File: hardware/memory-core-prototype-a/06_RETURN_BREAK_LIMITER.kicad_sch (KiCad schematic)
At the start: 1 part, among them J906 SHEET_INTERFACE_NOT_FITTED

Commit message: Capture ERC-validated Return Break limiter sheet
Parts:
- removed J906: SHEET_INTERFACE_NOT_FITTED, symbol Connector_Generic:Conn_01x07
- added C600: 1.2nF stability, Capacitor_SMD:C_0805_2012Metric, symbol Device:C
- added C601: 100nF V+, Capacitor_SMD:C_0805_2012Metric, symbol Device:C
- added C6010, C606: 4.7uF - rail, Capacitor_SMD:C_0805_2012Metric, symbol Device:C
- added C602: 100nF V-, Capacitor_SMD:C_0805_2012Metric, symbol Device:C
- added C603, C607: 100nF + rail, Capacitor_SMD:C_0805_2012Metric, symbol Device:C
- added C604, C608: 100nF - rail, Capacitor_SMD:C_0805_2012Metric, symbol Device:C
- added C605, C609: 4.7uF + rail, Capacitor_SMD:C_0805_2012Metric, symbol Device:C
- added C611: 100pF I/V, Capacitor_SMD:C_0805_2012Metric, symbol Device:C
- added C612: 1nF Break blur, Capacitor_SMD:C_0805_2012Metric, symbol Device:C
- added C613: 1uF +ref, Capacitor_SMD:C_0805_2012Metric, symbol Device:C
- added C614: 1uF -ref, Capacitor_SMD:C_0805_2012Metric, symbol Device:C
- added C615: 4.7uF release, Capacitor_SMD:C_0805_2012Metric, symbol Device:C
- added D600, D601: BAV199-class soft clip, symbol Device:D
- added D602: BAT54-class high clamp, symbol Device:D_Schottky
- added D603: BAT54-class low clamp, symbol Device:D_Schottky
- added D604: BAT54-class precision rectifier, symbol Device:D_Schottky
- added D605: 3.0V control clamp provisional, symbol Device:D_Zener
- added R600: 20k input, Resistor_SMD:R_0805_2012Metric, symbol Device:R
- added R601: 220R stability, Resistor_SMD:R_0805_2012Metric, symbol Device:R
- added R602: 20k I/V, Resistor_SMD:R_0805_2012Metric, symbol Device:R
- added R603: 22k Break input, Resistor_SMD:R_0805_2012Metric, symbol Device:R
- added R604: 22k Break feedback, Resistor_SMD:R_0805_2012Metric, symbol Device:R
- added R605: 22k normalise input, Resistor_SMD:R_0805_2012Metric, symbol Device:R
- added R606: 22k normalise feedback, Resistor_SMD:R_0805_2012Metric, symbol Device:R
- added R607: 38k +ref top, Resistor_SMD:R_0805_2012Metric, symbol Device:R
- added R608: 10k +ref bottom, Resistor_SMD:R_0805_2012Metric, symbol Device:R
- added R609: 38k -ref top, Resistor_SMD:R_0805_2012Metric, symbol Device:R
- added R610: 10k -ref bottom, Resistor_SMD:R_0805_2012Metric, symbol Device:R
- added R611: 2.2k, Resistor_SMD:R_0805_2012Metric, symbol Device:R
- added R612: 40.2k, Resistor_SMD:R_0805_2012Metric, symbol Device:R
- added R613: 27.4k, Resistor_SMD:R_0805_2012Metric, symbol Device:R
- added R614: 10k attack, Resistor_SMD:R_0805_2012Metric, symbol Device:R
- added R615: 220k release, Resistor_SMD:R_0805_2012Metric, symbol Device:R
- added TP600: RETURN_DAC, symbol Connector:TestPoint
- added TP601: RETURN_VCA, symbol Connector:TestPoint
- added TP602: BREAK_OUT, symbol Connector:TestPoint
- added TP603: RETURN_NORM, symbol Connector:TestPoint
- added TP604: +2V5_REF, symbol Connector:TestPoint
- added TP605: -2V5_REF, symbol Connector:TestPoint
- added TP606: RETURN_LIMITED, symbol Connector:TestPoint
- added TP607: RETURN_FEED, symbol Connector:TestPoint
- added TP608: ABSENCE_INFLUENCE, symbol Connector:TestPoint
- added TP609: VCA_RETURN_CTRL, symbol Connector:TestPoint
- added U50: SSI2164, symbol MerrinLab_PrototypeA:SSI2164S_APPLICATION
- added U60: OPA1679 RETURN A, symbol MerrinLab_PrototypeA:OPA1679_PW_APPLICATION
- added U61: OPA1679 RETURN B, symbol MerrinLab_PrototypeA:OPA1679_PW_APPLICATION
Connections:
- net ABSENCE_INFLUENCE: now also C615.1, D605.1 (K), R614.2, R615.1, TP608.1
- net RAIL_N12: now also C6010.1, C602.1, C604.1, C606.1, C608.1, R609.1, U50.9 (V-), U60.11 (V-), U61.11 (V-)
- net RAIL_P12: now also C601.1, C603.1, C605.1, C607.1, C609.1, R607.1, U50.16 (V+), U60.4 (V+), U61.4 (V+)
- net RETURN_DAC: now also R600.1, TP600.1
- net RETURN_FEED: now also R613.1, TP607.1, U61.8 (OUT_C)
- net RETURN_LIMITED: now also R612.1, TP606.1, U61.12 (IN_D+), U61.6 (IN_B-), U61.7 (OUT_B)
- net VCA_RETURN_CTRL: now also TP609.1, U50.11 (VC3)
- new net ABS_RECT: D604.1 (K), R614.1, U61.13 (IN_D-)
- new net ABS_RECT_DRIVE: D604.2 (A), U61.14 (OUT_D)
- new net BREAK_OUT: C612.1, D600.1 (K), D601.2 (A), R604.1, R605.1, TP602.1, U60.7 (OUT_B)
- new net BREAK_SUM: C612.2, D600.2 (A), D601.1 (K), R603.2, R604.2, U60.6 (IN_B-)
- new net GND: C600.2, C601.2, C6010.2, C602.2, C603.2, C604.2, C605.2, C606.2, C607.2, C608.2, C609.2, C613.2, C614.2, C615.2, D605.2 (A), R608.2, R610.2, R615.2, U50.8 (GND), U60.10 (IN_C+), U60.3 (IN_A+), U60.5 (IN_B+), U61.10 (IN_C+)
- new net REF_N2V5: D603.2 (A), TP605.1, U61.1 (OUT_A), U61.2 (IN_A-)
- new net REF_N_DIV: C614.1, R609.2, R610.1, U61.3 (IN_A+)
- new net REF_P2V5: D602.1 (K), TP604.1, U60.13 (IN_D-), U60.14 (OUT_D)
- new net REF_P_DIV: C613.1, R607.2, R608.1, U60.12 (IN_D+)
- new net RETFEED_SUM: R612.2, R613.2, U61.9 (IN_C-)
- new net RETURN_CLAMP: D602.2 (A), D603.1 (K), R611.2, U61.5 (IN_B+)
- new net RETURN_NORM: R606.1, R611.1, TP603.1, U60.8 (OUT_C)
- new net RETURN_VCA: C611.1, R602.1, R603.1, TP601.1, U60.1 (OUT_A)
- new net RET_NORM_SUM: R605.2, R606.2, U60.9 (IN_C-)
- new net SSI_IIN3: R600.2, R601.1, U50.10 (IIN3)
- new net SSI_IOUT3: C611.2, R602.2, U50.12 (IOUT3), U60.2 (IN_A-)
- new net SSI_RC3: C600.1, R601.2
- no-connect marks 0 -> 10
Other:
- note added: "Clamp references +/-2.5 V plus Schottky Vf give approximately 5.4-5.6 Vpp RETURN_LIMITED. Fixed feed magnitude = 27.4k / 40.2k = 0.6816; 1% worst case < 0.696."
- note added: "SSI2164 CH3: pins 10 IIN3, 11 VC3, 12 IOUT3. MODE pin 1 open = Class AB. Current output is converted by U60A; it is not treated as a voltage output."
- note added: "SSI2164 RETURN VCA • BOUNDED BREAK • INDEPENDENT HARD CLAMP • FIXED FEED"
- note added: "Small-signal path: SSI VCA <= unity; Break = -1; normaliser = -1. Only RETURN_LIMITED, RETURN_FEED and bounded ABSENCE_INFLUENCE cross this sheet."
- note added: "U50 units A/B/D are reserved no-connect placeholders on sheet 06. Sheet 05 must remove these placeholders and place the real Memory/Ghost/Wet channels."
- note added: "U50/U60/U61 and clamp-diode footprints intentionally blank. Exact diode leakage/Vf, reference source/sink current, measured loop gain and 30-minute endurance remain gates."
- note removed: "HIERARCHY / INTERFACE CAPTURE ONLY — CIRCUIT CONTENT NOT YET ACCEPTED"
- title: Memory Core Prototype A — RETURN / BREAK / LIMITER -> Memory Core Prototype A — Return / Break / Limiter

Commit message: Capture ERC-validated Return Break limiter sheet
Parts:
- removed C6010, C606: 4.7uF - rail, Capacitor_SMD:C_0805_2012Metric, symbol Device:C
- removed C602: 100nF V-, Capacitor_SMD:C_0805_2012Metric, symbol Device:C
- removed C604, C608: 100nF - rail, Capacitor_SMD:C_0805_2012Metric, symbol Device:C
- removed C605, C609: 4.7uF + rail, Capacitor_SMD:C_0805_2012Metric, symbol Device:C
- removed C607: 100nF + rail, Capacitor_SMD:C_0805_2012Metric, symbol Device:C
- removed D600, D601: BAV199-class soft clip, symbol Device:D
- removed D602: BAT54-class high clamp, symbol Device:D_Schottky
- removed D603: BAT54-class low clamp, symbol Device:D_Schottky
- removed D604: BAT54-class precision rectifier, symbol Device:D_Schottky
- removed D605: 3.0V control clamp provisional, symbol Device:D_Zener
- removed R606: 22k normalise feedback, Resistor_SMD:R_0805_2012Metric, symbol Device:R
- removed R607: 38k +ref top, Resistor_SMD:R_0805_2012Metric, symbol Device:R
- removed R608: 10k +ref bottom, Resistor_SMD:R_0805_2012Metric, symbol Device:R
- removed R609: 38k -ref top, Resistor_SMD:R_0805_2012Metric, symbol Device:R
- removed R615: 220k release, Resistor_SMD:R_0805_2012Metric, symbol Device:R
- removed U50: SSI2164, symbol MerrinLab_PrototypeA:SSI2164S_APPLICATION
- removed U60: OPA1679 RETURN A, symbol MerrinLab_PrototypeA:OPA1679_PW_APPLICATION
- added C610: 100nF + rail, Capacitor_SMD:C_0805_2012Metric, symbol Device:C
- added C616: 4.7uF + rail, Capacitor_SMD:C_0805_2012Metric, symbol Device:C
- added C617: 4.7uF - rail, Capacitor_SMD:C_0805_2012Metric, symbol Device:C
- added C618: 100nF SSI + rail, Capacitor_SMD:C_0805_2012Metric, symbol Device:C
- added C619: 100nF SSI - rail, Capacitor_SMD:C_0805_2012Metric, symbol Device:C
- added C620, C621: 1uF, Capacitor_SMD:C_0805_2012Metric, symbol Device:C
- added C630: 1uF attack/release, Capacitor_SMD:C_0805_2012Metric, symbol Device:C
- added C640: 330pF bandwidth, Capacitor_SMD:C_0805_2012Metric, symbol Device:C
- added C641: 390pF bandwidth loss, Capacitor_SMD:C_0805_2012Metric, symbol Device:C
- added D600, D610: BAT54-class upper clamp, symbol Device:D_Schottky
- added D601, D611: BAT54-class lower clamp, symbol Device:D_Schottky
- added D602: Break diode A, symbol Device:D
- added D603: Break diode B, symbol Device:D
- added D604: Asym single, symbol Device:D
- added D605: Asym pair 1, symbol Device:D
- added D606: Asym pair 2, symbol Device:D
- added D607: Upper hard clamp, symbol Device:D_Schottky
- added D608: Lower hard clamp, symbol Device:D_Schottky
- added D609: Envelope rectifier, symbol Device:D_Schottky
- added D612: Fault-neutral clamp, symbol Device:D_Schottky
- added R620, R622: 38.3k 1%, Resistor_SMD:R_0805_2012Metric, symbol Device:R
- added R621, R623: 10k 1%, Resistor_SMD:R_0805_2012Metric, symbol Device:R
- added R624: 2.2k clamp current, Resistor_SMD:R_0805_2012Metric, symbol Device:R
- added R625: 47R output isolate, Resistor_SMD:R_0805_2012Metric, symbol Device:R
- added R626: 40.2k 1%, Resistor_SMD:R_0805_2012Metric, symbol Device:R
- added R627: 27.4k 1%, Resistor_SMD:R_0805_2012Metric, symbol Device:R
- added R630: 10k rectifier feed, Resistor_SMD:R_0805_2012Metric, symbol Device:R
- added R631: 100k release, Resistor_SMD:R_0805_2012Metric, symbol Device:R
- added R632: 1k output isolate, Resistor_SMD:R_0805_2012Metric, symbol Device:R
- added R633: 100k neutral pull-down, Resistor_SMD:R_0805_2012Metric, symbol Device:R
- added RV60: 100k BREAK AMOUNT, symbol MerrinLab_PrototypeA:R_POT_123
- added TP610: SSI_VC3, symbol Connector:TestPoint
- added U60: SSI2164, symbol MerrinLab_PrototypeA:SSI2164S_MULTI
- added U62: OPA1679 REFERENCES / ABSENCE, symbol MerrinLab_PrototypeA:OPA1679_PW_APPLICATION
- C600: value 1.2nF stability -> 10uF AC; footprint Capacitor_SMD:C_0805_2012Metric -> (none)
- C601: value 100nF V+ -> 1.2nF stability
- C603: value 100nF + rail -> 100pF I/V
- C611: value 100pF I/V -> 100nF - rail
- C612: value 1nF Break blur -> 4.7uF + rail
- C613: value 1uF +ref -> 4.7uF - rail
- C614: value 1uF -ref -> 100nF + rail
- C615: value 4.7uF release -> 100nF - rail
- R600: value 20k input -> 20k
- R601: value 220R stability -> 10k
- R602: value 20k I/V -> 20k SSI input
- R603: value 22k Break input -> 220R stability
- R604: value 22k Break feedback -> 1k control isolate
- R605: value 22k normalise input -> 20k I/V
- R610: value 10k -ref bottom -> 20k
- R611: value 2.2k -> 20k unity feedback
- R612: value 40.2k -> 20k
- R613: value 27.4k -> 20k unity feedback
- R614: value 10k attack -> 6.8k nonlinear feed
- TP601: value RETURN_VCA -> RETURN_NORM
- TP602: value BREAK_OUT -> RETURN_VCA
- TP603: value RETURN_NORM -> BREAK
- TP604: value +2V5_REF -> RETURN_NONLINEAR
- TP605: value -2V5_REF -> +2V5_REF
- TP606: value RETURN_LIMITED -> -2V5_REF
- TP607: value RETURN_FEED -> RETURN_LIMITED
- TP608: value ABSENCE_INFLUENCE -> RETURN_FEED
- TP609: value VCA_RETURN_CTRL -> ABSENCE_INFLUENCE
- U61: value OPA1679 RETURN B -> OPA1679 RETURN AUDIO
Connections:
- net ABS_RECT_DRIVE is gone; now on net RET_LIM_BUF: U61.14 (OUT_D)
- net REF_P_DIV is gone; now on net RAIL_N12: C613.1
- net RET_NORM_SUM is gone; now on net SSI_IOUT3: R605.2
- net ABSENCE_INFLUENCE: now also TP609.1, D610.2 (A), D611.1 (K), D612.2 (A), R632.2, R633.1; no longer C615.1, R614.2, TP608.1
- net GND: now also C611.2, C612.2, R601.2, U61.3 (IN_A+), U61.5 (IN_B+), C610.2, C616.2, C617.2, C618.2, C619.2, C620.2, C621.2, C630.2, D601.2 (A), D611.2 (A), R621.2, R623.2, R631.2, R633.2, U60.8 (GND), U62.10 (IN_C+); no longer C600.2, C603.2, R610.2
- net RAIL_N12: now also C611.1, C615.1, C617.1, C619.1, R622.1, U60.9 (V-), U62.11 (V-)
- net RAIL_P12: now also C612.1, C614.1, C610.1, C616.1, C618.1, R620.1, U60.16 (V+), U62.4 (V+); no longer C601.1, C603.1
- net REF_N2V5: now also TP606.1, D608.2 (A), U62.6 (IN_B-), U62.7 (OUT_B); no longer TP605.1, U61.1 (OUT_A), U61.2 (IN_A-)
- net REF_P2V5: now also TP605.1, D607.1 (K), U62.1 (OUT_A), U62.2 (IN_A-); no longer TP604.1
- net RETFEED_SUM: now also R626.2, R627.2, U62.9 (IN_C-); no longer R612.2, R613.2, U61.9 (IN_C-)
- net RETURN_FEED: now also TP608.1, R627.1, U62.8 (OUT_C); no longer R613.1, TP607.1, U61.8 (OUT_C)
- net RETURN_LIMITED: now also TP607.1, R625.2, R626.1, R630.1; no longer R612.1, TP606.1, U61.12 (IN_D+), U61.6 (IN_B-), U61.7 (OUT_B)
- net RETURN_VCA: now also C603.1, R605.1, R610.1, TP602.1, U61.1 (OUT_A); no longer C611.1, R602.1, R603.1, TP601.1
- net SSI_IIN3: now also R602.2, R603.1, U60.15 (IIN3); no longer R600.2, R601.1
- net SSI_IOUT3: now also C603.2, U61.2 (IN_A-), U60.13 (IOUT3); no longer C611.2, R602.2
- net VCA_RETURN_CTRL: now also R604.1; no longer TP609.1
- net ABS_RECT renamed RET_LIM_BUF
- net RET_LIM_BUF: now also R625.1; no longer R614.1
- removed net BREAK_OUT: C612.1, R604.1, R605.1, TP602.1
- removed net BREAK_SUM: C612.2, R603.2, R604.2
- removed net REF_N_DIV: C614.1, R610.1, U61.3 (IN_A+)
- net RETURN_CLAMP renamed BRK_SUM
- net BRK_SUM: now also R610.2, U61.6 (IN_B-), C640.2, RV60.3 (END_B); no longer U61.5 (IN_B+)
- net RETURN_NORM renamed BRK_OUT
- net BRK_OUT: now also R612.1, U61.7 (OUT_B), C640.1, D602.1 (K), D603.2 (A)
- net SSI_RC3 renamed RETURN_DIV
- net RETURN_DIV: now also R600.2, R601.1, TP601.1; no longer R601.2
- new net ABS_CTRL_DRV: R632.1, U62.13 (IN_D-), U62.14 (OUT_D)
- new net ABS_ENV_RAW: C630.1, D609.1 (K), R631.1, U62.12 (IN_D+)
- new net ABS_RECT_IN: D609.2 (A), R630.2
- new net BRK_DIODE: D602.2 (A), D603.1 (K), RV60.1 (END_A), RV60.2 (WIPER)
- new net HARDWARE_FAULT_N: D612.1 (K)
- new net RAIL_3V3: D600.1 (K), D610.1 (K)
- new net REFN_DIV: C621.1, R622.2, R623.1, U62.5 (IN_B+)
- new net REFP_DIV: C620.1, R620.2, R621.1, U62.3 (IN_A+)
- new net RETURN_VCA_AC: C600.2, R602.1
- new net RET_ASYM_A: D604.2 (A), D605.1 (K), R614.2
- new net RET_ASYM_B: D605.2 (A), D606.1 (K)
- new net RET_CLAMP_NODE: D607.2 (A), D608.1 (K), R624.2, U61.12 (IN_D+)
- new net RET_NL_OUT: C641.1, R613.1, R614.1, R624.1, TP604.1, U61.8 (OUT_C)
- new net RET_SUM: C641.2, D604.1 (K), D606.2 (A), R612.2, R613.2, U61.9 (IN_C-)
- new net SSI_STAB3: C601.1, R603.2
- new net SSI_VC3: D600.2 (A), D601.1 (K), R604.2, TP610.1, U60.14 (VC3)
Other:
- note added: "FIXED FEED: 27.4k / 40.2k = 0.6816 nominal; 1% worst case <0.696. Only RETURN_LIMITED, RETURN_FEED and ABSENCE_INFLUENCE cross this boundary."
- note added: "GAIN CONTRACT sheet-03 Return receiver ~0.747; R600/R601 = 1/3; combined ~0.249. SSI2164 VC3 is restricted to 0…3.3 V, so VCA gain cannot exceed unity. Break and RET-01 are unity at small signal; nonlinear branches alter shape, not linear gain."
- note added: "HARD LIMITER R624 limits clamp current. D607/D608 clamp to buffered +/-2.5 V references. Expected first-pass limit ~+/-2.7…2.8 V. Limiter remains analogue and MCU-independent."
- note added: "Official SSI2164 channel 3 pins: 15 IIN3, 14 VC3, 13 IOUT3. Pins 10/11/12 are channel 4 and are reserved for the wet-master unit on sheet 05."
- note added: "SSI2164 CH3 • VARIABLE BREAK • UNITY-NORMALISED RETURN • INDEPENDENT ANALOGUE CLAMP"
- note added: "U60 units 1, 2 and 4 are visible staged reservations for sheet 05. They are the same physical SSI2164 as units 3 and 5, not duplicate chips. Sheet 05 must remove these reservations and place the real Memory/Ghost/Wet circuits."
- note removed: "Clamp references +/-2.5 V plus Schottky Vf give approximately 5.4-5.6 Vpp RETURN_LIMITED. Fixed feed magnitude = 27.4k / 40.2k = 0.6816; 1% worst case < 0.696."
- note removed: "SSI2164 CH3: pins 10 IIN3, 11 VC3, 12 IOUT3. MODE pin 1 open = Class AB. Current output is converted by U60A; it is not treated as a voltage output."
- note removed: "SSI2164 RETURN VCA • BOUNDED BREAK • INDEPENDENT HARD CLAMP • FIXED FEED"
- note removed: "Small-signal path: SSI VCA <= unity; Break = -1; normaliser = -1. Only RETURN_LIMITED, RETURN_FEED and bounded ABSENCE_INFLUENCE cross this sheet."
- note removed: "U50 units A/B/D are reserved no-connect placeholders on sheet 06. Sheet 05 must remove these placeholders and place the real Memory/Ghost/Wet channels."
- note removed: "U50/U60/U61 and clamp-diode footprints intentionally blank. Exact diode leakage/Vf, reference source/sink current, measured loop gain and 30-minute endurance remain gates."

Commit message: Capture ERC-validated Memory Ghost wet sheet
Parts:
- removed unit 1 of U60
- removed unit 2 of U60
- removed unit 4 of U60
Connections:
- no-connect marks 10 -> 1
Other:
- note removed: "U60 units 1, 2 and 4 are visible staged reservations for sheet 05. They are the same physical SSI2164 as units 3 and 5, not duplicate chips. Sheet 05 must remove these reservations and place the real Memory/Ghost/Wet circuits."

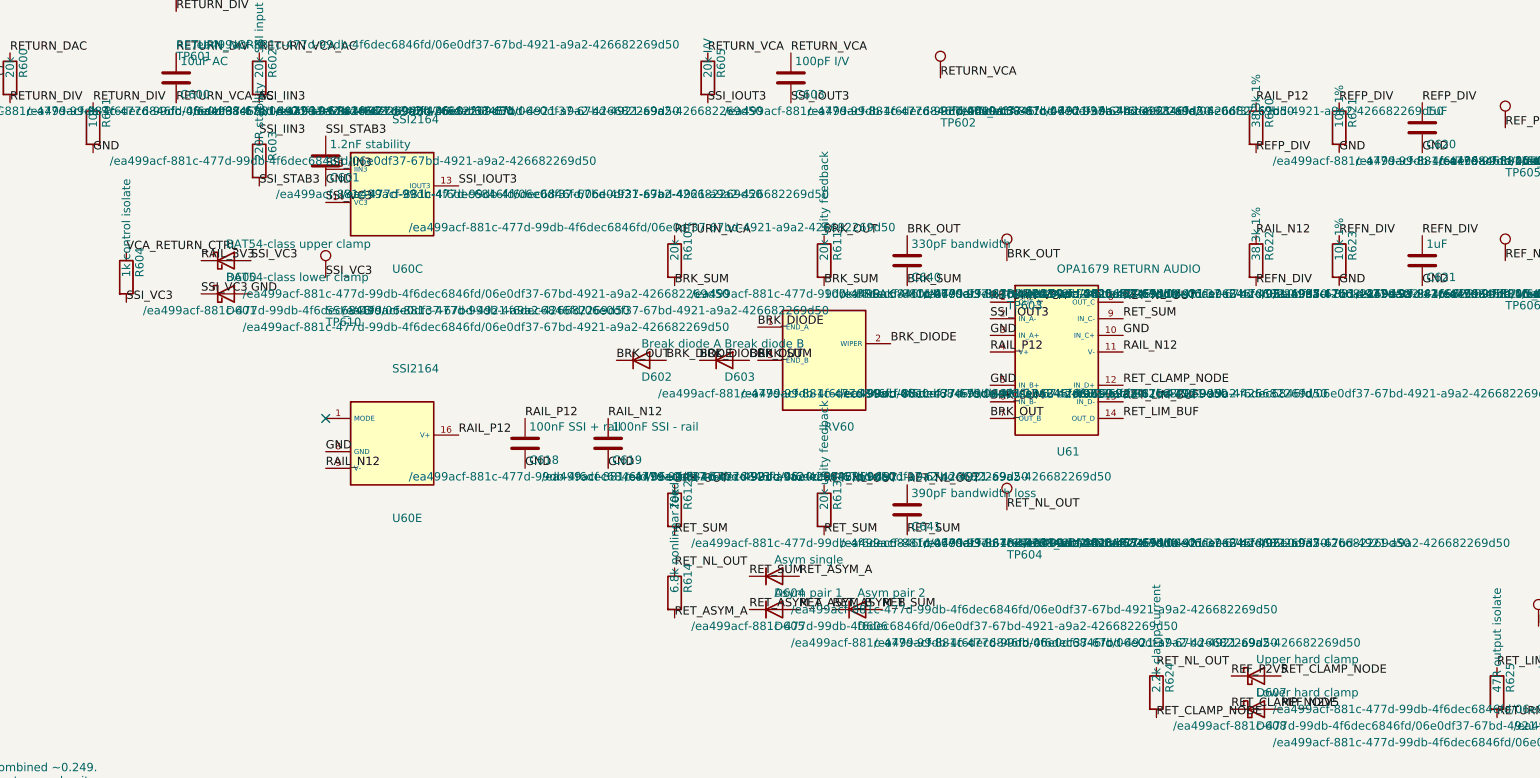
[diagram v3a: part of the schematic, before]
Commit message: Implement validated SSI2164 buffered control
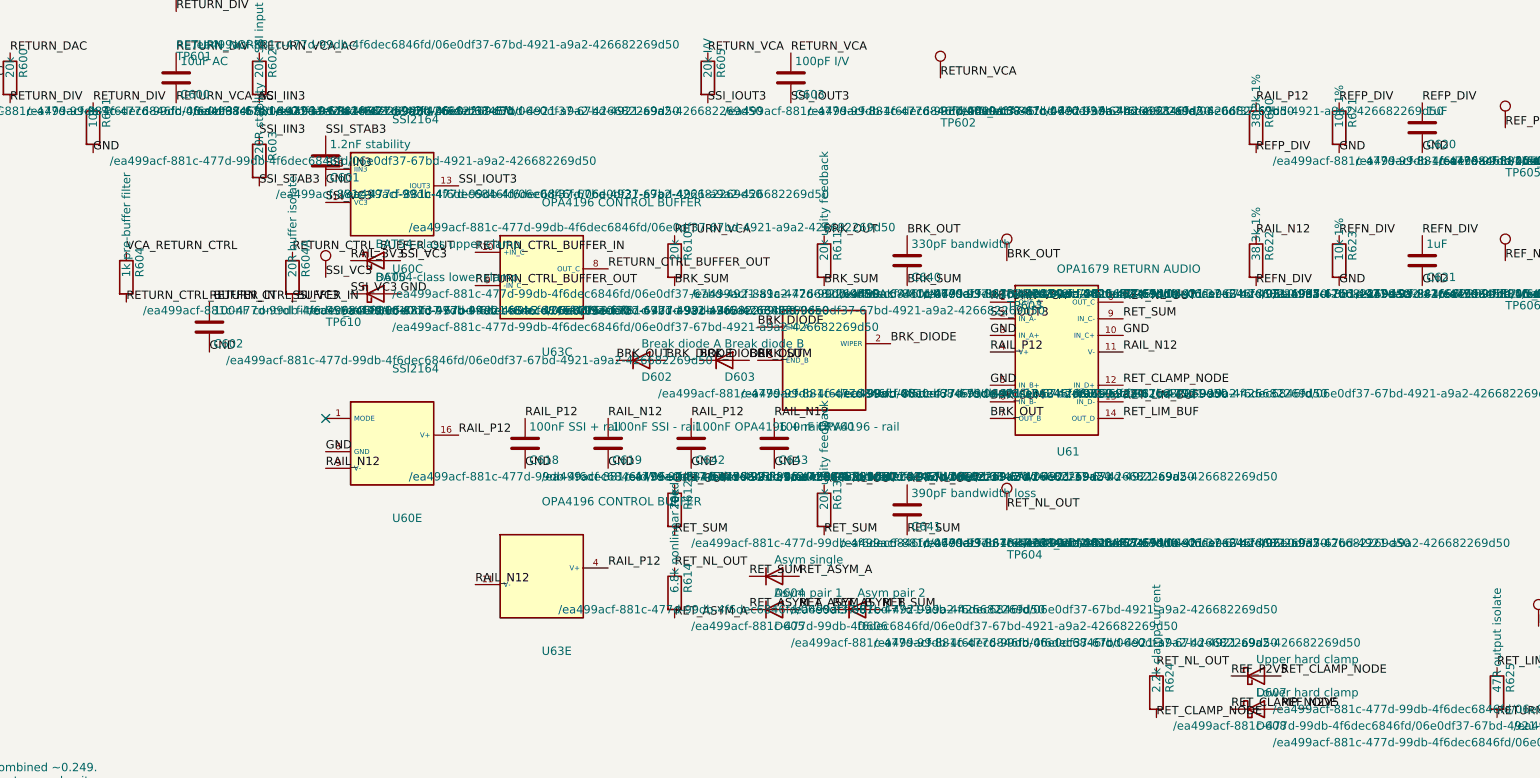
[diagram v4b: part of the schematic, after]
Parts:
- added C602: 100nF control filter, Capacitor_SMD:C_0805_2012Metric, symbol Device:C
- added C642: 100nF OPA4196 + rail, Capacitor_SMD:C_0805_2012Metric, symbol Device:C
- added C643: 100nF OPA4196 - rail, Capacitor_SMD:C_0805_2012Metric, symbol Device:C
- added R604A: 20R buffer isolate, Resistor_SMD:R_0805_2012Metric, symbol Device:R
- added U63: OPA4196 CONTROL BUFFER, symbol MerrinLab_PrototypeA:OPA4196_PW_MULTI
- R604: value 1k control isolate -> 1k pre-buffer filter
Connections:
- net GND: now also C602.2, C642.2, C643.2
- net RAIL_N12: now also C643.1, U63.11 (V-)
- net RAIL_P12: now also C642.1, U63.4 (V+)
- net SSI_VC3: now also R604A.2; no longer R604.2
- new net RETURN_CTRL_BUFFER_IN: C602.1, R604.2, U63.10 (+IN_C)
- new net RETURN_CTRL_BUFFER_OUT: R604A.1, U63.8 (OUT_C), U63.9 (-IN_C)
